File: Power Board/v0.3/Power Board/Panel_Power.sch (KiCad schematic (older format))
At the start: 0 parts

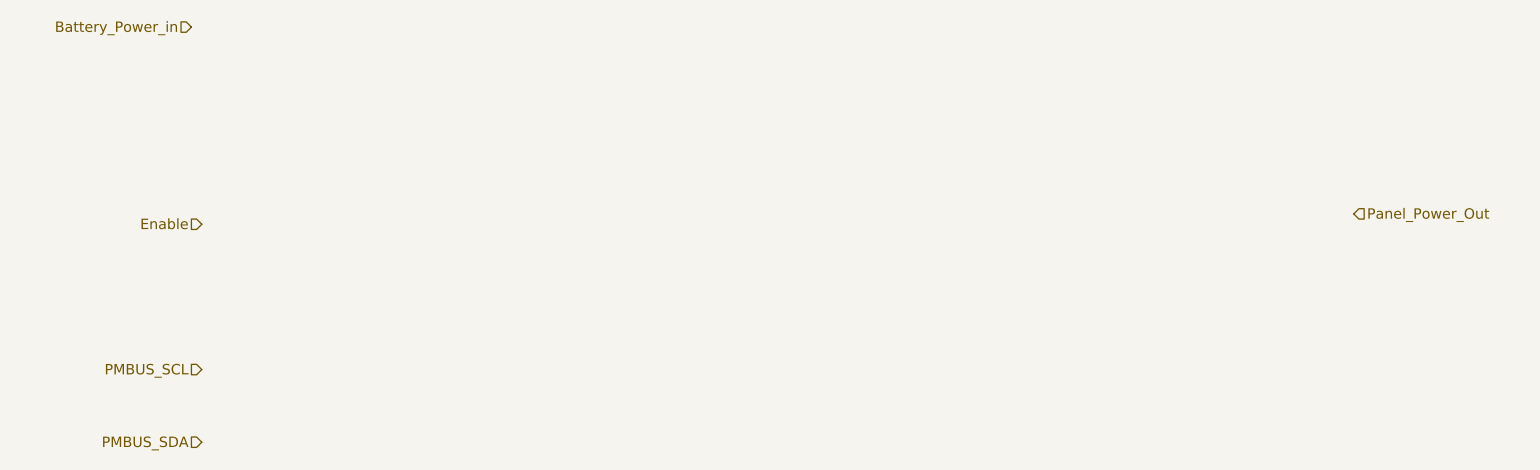
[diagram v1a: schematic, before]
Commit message: Merge Pi_Power schematic into Soft_Switch.
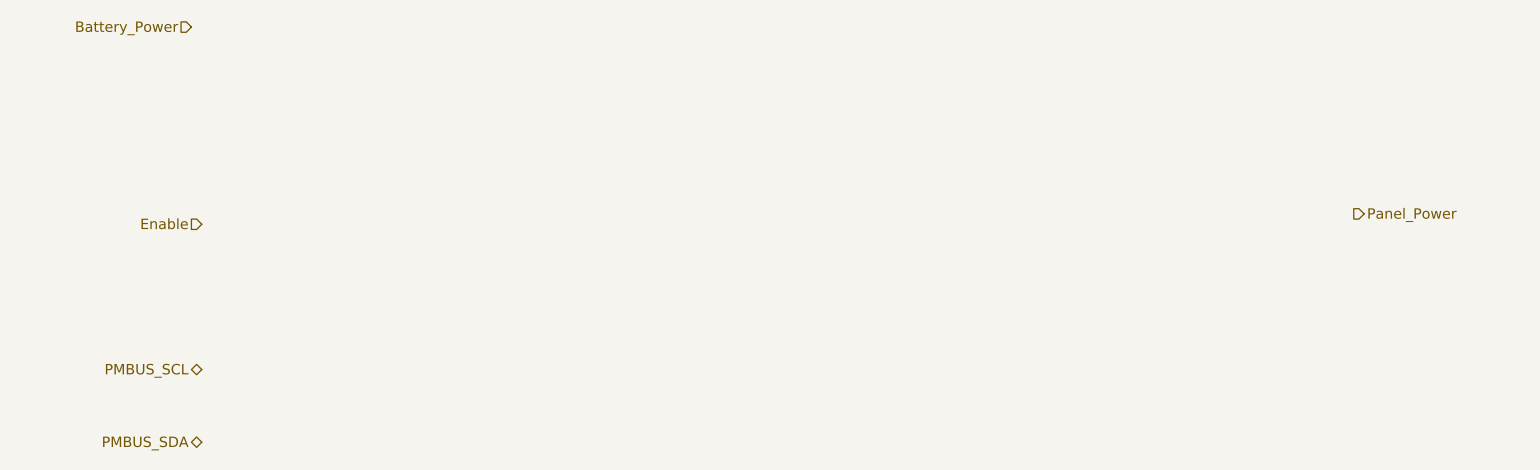
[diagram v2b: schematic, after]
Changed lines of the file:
@@
 $Descr A4 11693 8268
 encoding utf-8
-Sheet 2 4
+Sheet 2 3
 Title ""
 Date ""
@@
 $EndDescr
 Text HLabel 2550 2600 0    50   Input ~ 0
-Battery_Power_in
+Battery_Power
 Text HLabel 2600 3550 0    50   Input ~ 0
 Enable
-Text HLabel 2600 4250 0    50   Input ~ 0
+Text HLabel 2600 4250 0    50   BiDi ~ 0
 PMBUS_SCL
-Text HLabel 2600 4600 0    50   Input ~ 0
+Text HLabel 2600 4600 0    50   BiDi ~ 0
 PMBUS_SDA
-Text HLabel 8150 3500 2    50   Input ~ 0
-Panel_Power_Out
+Text HLabel 8150 3500 2    50   Output ~ 0
+Panel_Power
 $EndSCHEMATC

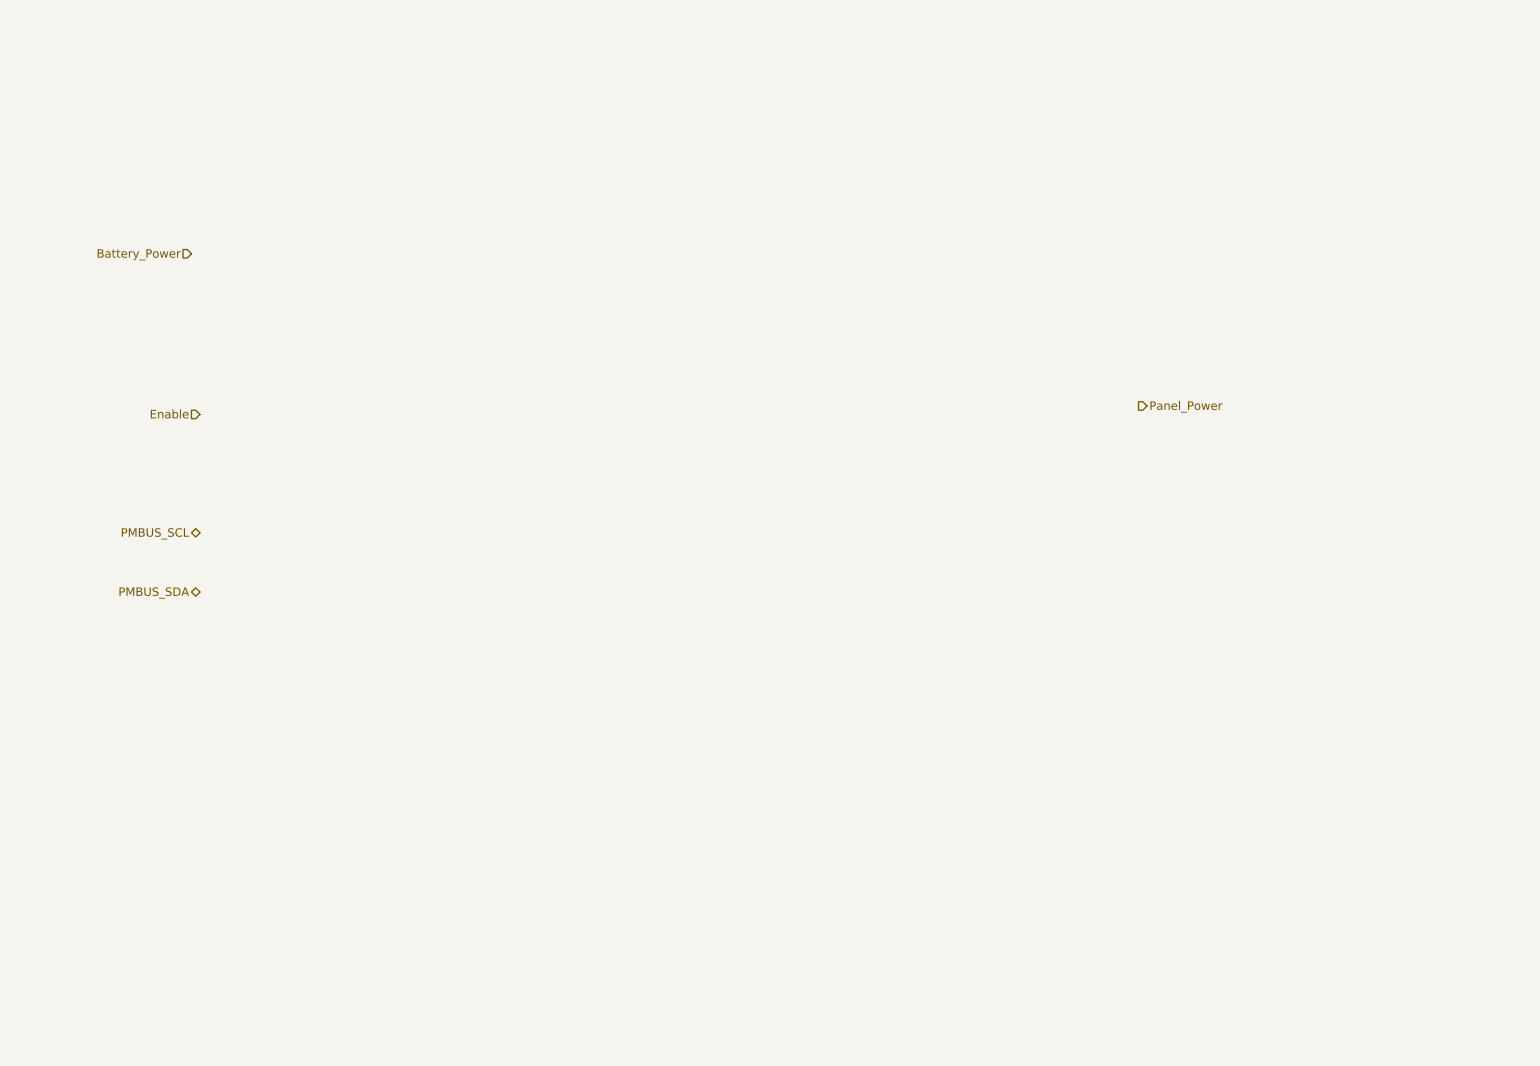
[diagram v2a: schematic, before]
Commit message: Create the LED panel supply circuit.
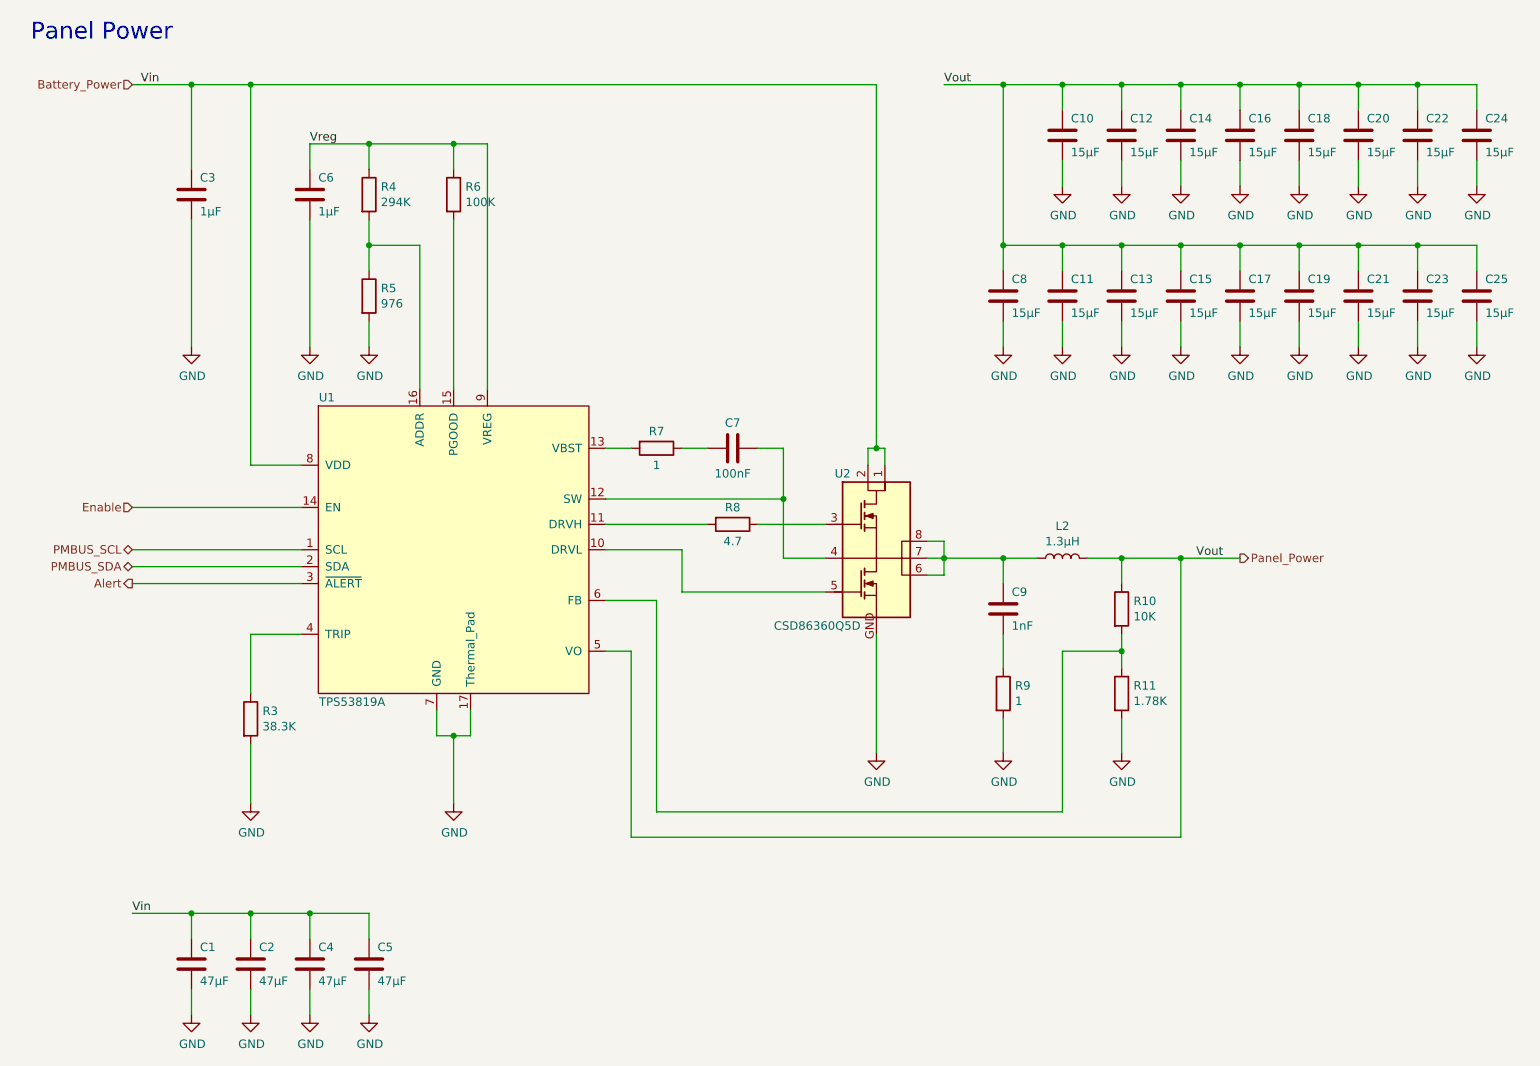
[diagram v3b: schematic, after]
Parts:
- added C1, C2, C4, C5: 47µF, Capacitor_SMD:C_1206_3216Metric, symbol Device:C
- added C10, C11, C12, C13, C14, C15, C16, C17, C18, C19, C20, C21, C22, C23, C24, C25, C8: 15µF, Capacitor_SMD:C_0805_2012Metric, symbol Device:C
- added C3, C6: 1µF, Capacitor_SMD:C_0805_2012Metric, symbol Device:C
- added C7: 100nF, Capacitor_SMD:C_0805_2012Metric, symbol Device:C
- added C9: 1nF, Capacitor_SMD:C_0603_1608Metric, symbol Device:C
- added L2: 1.3µH, symbol Device:L
- added R10: 10K, Resistor_SMD:R_0402_1005Metric, symbol Device:R
- added R11: 1.78K, Resistor_SMD:R_0805_2012Metric, symbol Device:R
- added R3: 38.3K, Resistor_SMD:R_0805_2012Metric, symbol Device:R
- added R4: 294K, Resistor_SMD:R_0402_1005Metric, symbol Device:R
- added R5: 976, Resistor_SMD:R_0402_1005Metric, symbol Device:R
- added R6: 100K, Resistor_SMD:R_0603_1608Metric, symbol Device:R
- added R7, R9: 1, Resistor_SMD:R_0805_2012Metric, symbol Device:R
- added R8: 4.7, Resistor_SMD:R_0805_2012Metric, symbol Device:R
- added U1: TPS53819A, ~, symbol Power_Board:TPS53819A
- added U2: CSD86360Q5D, symbol Power_Board:CSD86360Q5D
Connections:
- net Battery_Power: now also C1.1, C2.1, C3.1, C4.1, C5.1, U1.8 (VDD), U2.1 (VIN), U2.2 (VIN)
- net Enable: now also U1.14 (EN)
- net PMBUS_SCL: now also U1.1 (SCL)
- net PMBUS_SDA: now also U1.2 (SDA)
- net Panel_Power: now also C10.1, C11.1, C12.1, C13.1, C14.1, C15.1, C16.1, C17.1, C18.1, C19.1, C20.1, C21.1, C22.1, C23.1, C24.1, C25.1, C8.1, L2.2, R10.1, U1.5 (VO)
- new net: R8.1, U2.3 (TG)
- new net: C7.1, U1.12 (SW), U2.4 (TGR)
- new net: U1.10 (DRVL), U2.5 (BG)
- new net: C9.1, L2.1, U2.6 (VSW), U2.7 (VSW), U2.8 (VSW)
- new net: R8.2, U1.11 (DRVH)
- new net: C7.2, R7.1
- new net: R7.2, U1.13 (VBST)
- new net: C9.2, R9.1
- new net: R10.2, R11.1, U1.6 (FB)
- new net: R6.2, U1.15 (PGOOD)
- new net: R4.2, R5.1, U1.16 (ADDR)
- new net: R3.1, U1.4 (TRIP)
- new net Alert: U1.3 (~ALERT)
- new net GND: C1.2, C10.2, C11.2, C12.2, C13.2, C14.2, C15.2, C16.2, C17.2, C18.2, C19.2, C2.2, C20.2, C21.2, C22.2, C23.2, C24.2, C25.2, C3.2, C4.2, C5.2, C6.2, C8.2, R11.2, R3.2, R5.2, R9.2, U1.17 (Thermal_Pad), U1.7 (GND), U2.GND (PGND)
- new net Vreg: C6.1, R4.1, R6.1, U1.9 (VREG)
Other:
- note added: "Panel Power"

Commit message: Update components with available parts.
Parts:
- removed C1, C4, C5: 47µF, Capacitor_SMD:C_1206_3216Metric, symbol Device:C
- removed C10, C11, C13, C14, C15, C16, C17, C18, C19, C20, C21, C22, C23, C24, C25, C8: 15µF, Capacitor_SMD:C_0805_2012Metric, symbol Device:C
- added C12: 100µF, symbol Device:CP1
- C13: renamed from C2; value 47µF -> 10µF; footprint Capacitor_SMD:C_1206_3216Metric -> Capacitor_SMD:C_0805_2012Metric; Digikey No. 445-8047-1-ND -> 490-10748-1-ND; Manufacturer TDK -> Murata; Part No. C3216X5R1E476M160AC -> GRM21BR61E106MA73L
- C14: renamed from C6; Digikey No. 587-1283-1-ND -> 587-1438-1-ND; Part No. EMK212B7105KG-T -> GMK212B7105KG-T
- C18: renamed from C12; value 15µF -> 10µF; Digikey No. 445-14423-1-ND -> 490-10748-1-ND; Manufacturer TDK -> Murata; Part No. C2012X5R1V156M125AC -> GRM21BR61E106MA73L
- L8: renamed from L2; Digikey No. not avail. -> Mouser
- R16: renamed from R6; Digikey No. (none) -> -
- renumbered C3 to C11, C7 to C15, C9 to C16, R3 to R13, R4 to R14, R5 to R15, R7 to R17, R8 to R18, R9 to R19, R10 to R20, R11 to R21, U1 to U2, U2 to U3
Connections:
- net Battery_Power: now also C12.1
- net GND: now also C12.2
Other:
- moved on the sheet: C18

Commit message: Draw all custom footprints and assign to components.
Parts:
- C12: footprint (none) -> Capacitor_SMD:CP_Elec_8x10
- L8: footprint (none) -> Power_Board:CP_Kemet_8.3x10
- R21: footprint Resistor_SMD:R_0805_2012Metric -> Power_Board:TO-PMOD_7
- U2: footprint ~ -> Package_DFN_QFN:VQFN-16-1EP_3x3mm_P0.5mm_EP1.68x1.68mm_ThermalVias
- U3: footprint (none) -> Power_Board:Q5D
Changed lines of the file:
@@
 F 0 "U2" H 3350 5250 50  0000 C CNN
 F 1 "TPS53819A" H 3500 3450 50  0000 C CNN
-F 2 "~" H 4100 4350 50  0001 C CNN
+F 2 "Package_DFN_QFN:VQFN-16-1EP_3x3mm_P0.5mm_EP1.68x1.68mm_ThermalVias" H 4100 4350 50  0001 C CNN
 F 3 "" H 4100 4350 50  0001 C CNN
 F 4 "TPS53819ARGTR" H -100 0   50  0001 C CNN "Part No."
@@
 F 0 "R21" H 8120 5246 50  0000 L CNN
 F 1 "1.78K" H 8120 5155 50  0000 L CNN
-F 2 "Resistor_SMD:R_0805_2012Metric" V 7980 5200 50  0001 C CNN
+F 2 "Power_Board:TO-PMOD_7" V 7980 5200 50  0001 C CNN
 F 3 "~" H 8050 5200 50  0001 C CNN
 F 4 "P1.78KCCT-ND" H 0   0   50  0001 C CNN "Digikey No."
@@
 F 0 "L8" V 7890 4400 50  0000 C CNN
 F 1 "1.3µH" V 7799 4400 50  0000 C CNN
-F 2 "" H 7700 4400 50  0001 C CNN
+F 2 "Power_Board:CP_Kemet_8.3x10" H 7700 4400 50  0001 C CNN
 F 3 "~" H 7700 4400 50  0001 C CNN
 F 4 "Mouser" H -100 0   50  0001 C CNN "Digikey No."
@@
 F 0 "U3" H 6400 4800 50  0000 C CNN
 F 1 "CSD86360Q5D" H 6250 3900 50  0000 C CNN
-F 2 "" H 6500 4350 100 0001 C CNN
+F 2 "Power_Board:Q5D" H 6500 4350 100 0001 C CNN
 F 3 "" H 6500 4350 100 0001 C CNN
 F 4 "TI" H 0   0   50  0001 C CNN "Manufacturer"
@@
 F 0 "C12" H 2600 6900 50  0000 L CNN
 F 1 "100µF" H 2600 6700 50  0000 L CNN
-F 2 "" H 2550 6800 50  0001 C CNN
-F 3 "~" H 2550 6800 50  0001 C CNN
+F 2 "Capacitor_SMD:CP_Elec_8x10" H 2550 6800 50  0001 C CNN
+F 3 "https://datasheet.octopart.com/EDK107M050A9MAA-Kemet-datasheet-13271990.pdf" H 2550 6800 50  0001 C CNN
 F 4 "399-6672-1-ND" H 0   0   50  0001 C CNN "Digikey No."
 F 5 "Kemet" H 0   0   50  0001 C CNN "Manufacturer"

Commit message: Work in progress.
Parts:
- R21: footprint Power_Board:TO-PMOD_7 -> Resistor_SMD:R_0805_2012Metric
- renumbered C18 to C17
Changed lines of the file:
@@
 Connection ~ 8400 4400
 $Comp
-L Device:C C18
+L Device:C C17
 U 1 1 5CA00DCF
 P 7700 1900
-F 0 "C18" H 7750 2000 50  0000 L CNN
+F 0 "C17" H 7750 2000 50  0000 L CNN
 F 1 "10µF" H 7750 1800 50  0000 L CNN
 F 2 "Capacitor_SMD:C_0805_2012Metric" H 7738 1750 50  0001 C CNN
@@
 F 0 "R21" H 8120 5246 50  0000 L CNN
 F 1 "1.78K" H 8120 5155 50  0000 L CNN
-F 2 "Power_Board:TO-PMOD_7" V 7980 5200 50  0001 C CNN
+F 2 "Resistor_SMD:R_0805_2012Metric" V 7980 5200 50  0001 C CNN
 F 3 "~" H 8050 5200 50  0001 C CNN
 F 4 "P1.78KCCT-ND" H 0   0   50  0001 C CNN "Digikey No."

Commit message: Work in progress.
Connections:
- net Drive_High_2: now reaches R18.1, U3.3 (TG)
- net Drive_Low: now reaches U2.10 (DRVL), U3.5 (BG)
- net Switch_Node: now reaches C16.1, L8.1, U3.6 (VSW), U3.7 (VSW), U3.8 (VSW)
- net Drive_High_1: now reaches R18.2, U2.11 (DRVH)
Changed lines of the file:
@@
 	1    0    0    -1
 $EndComp
+Text Label 7000 4300 0    50   ~ 0
+Switch_Node
+Text Label 5600 4600 0    50   ~ 0
+Drive_Low
+Text Label 5050 4200 0    50   ~ 0
+Drive_High_1
+Text Label 6250 4200 1    50   ~ 0
+Drive_High_2
 $EndSCHEMATC

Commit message: L8 footprint is Coilcraft XAL1580, not some Kemet cap.
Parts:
- L8: footprint Power_Board:CP_Kemet_8.3x10 -> Power_Board:Coilcraft_XAL1580
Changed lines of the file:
@@
 F 0 "L8" V 7890 4400 50  0000 C CNN
 F 1 "1.3µH" V 7799 4400 50  0000 C CNN
-F 2 "Power_Board:CP_Kemet_8.3x10" H 7700 4400 50  0001 C CNN
+F 2 "Power_Board:Coilcraft_XAL1580" H 7700 4400 50  0001 C CNN
 F 3 "~" H 7700 4400 50  0001 C CNN
 F 4 "Mouser" H -100 0   50  0001 C CNN "Digikey No."
